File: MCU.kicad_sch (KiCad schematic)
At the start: 10 parts, among them SW1 SW_Omron_B3FS, SW3 SW_Omron_B3FS, U1 ESP32-WROOM-32E, X1 SG-3030CM

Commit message: Started to layout PCB
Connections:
- net MCU_EN is gone; now on net EN: C1.1, R1.2

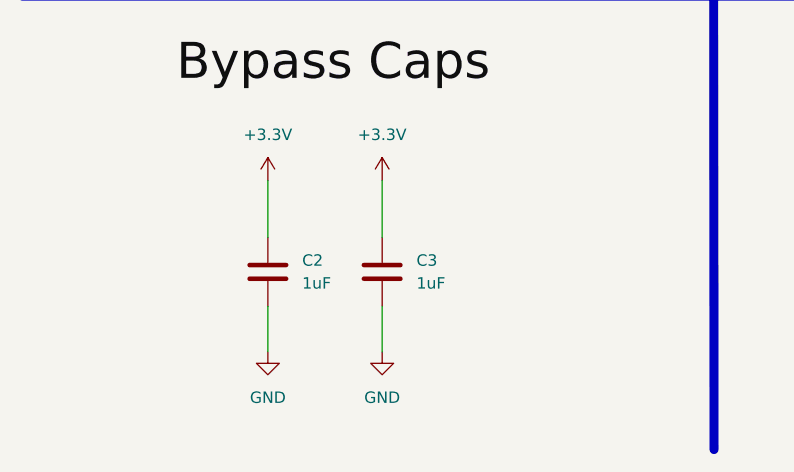
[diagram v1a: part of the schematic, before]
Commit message: Placed all components on PCB
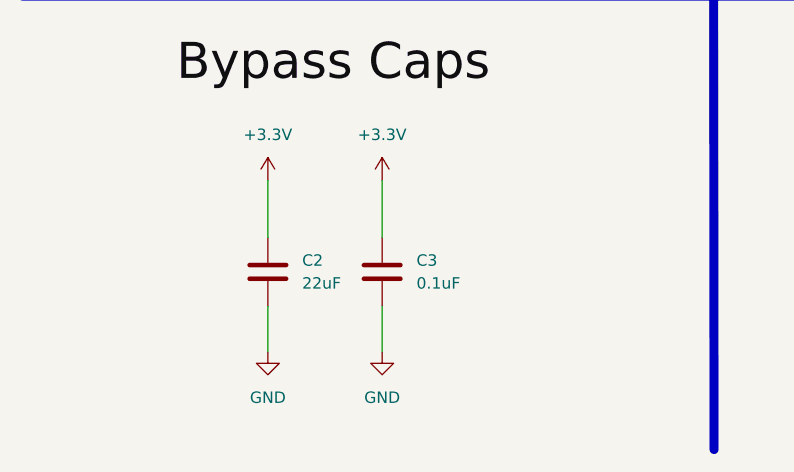
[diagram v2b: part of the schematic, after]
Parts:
- C2: value 1uF -> 22uF
- C3: value 1uF -> 0.1uF
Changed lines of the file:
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@@
 			)
 		)
-		(property "Value" "1uF"
+		(property "Value" "0.1uF"
 			(at 55.88 179.0699 0)
 			(effects
@@
 			)
 		)
-		(property "Value" "1uF"
+		(property "Value" "22uF"
 			(at 43.18 179.0699 0)
 			(effects

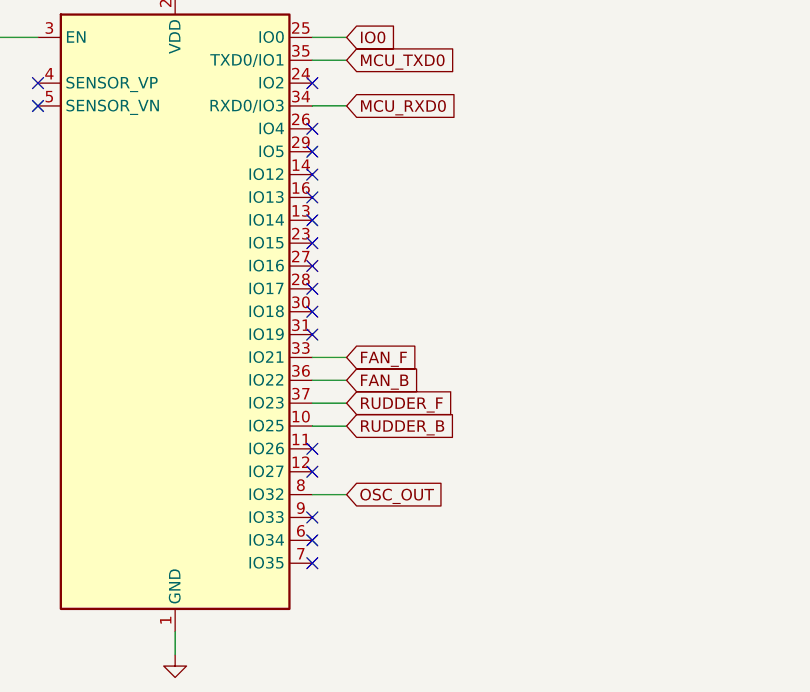
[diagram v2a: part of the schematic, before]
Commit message: Finished PCB routing
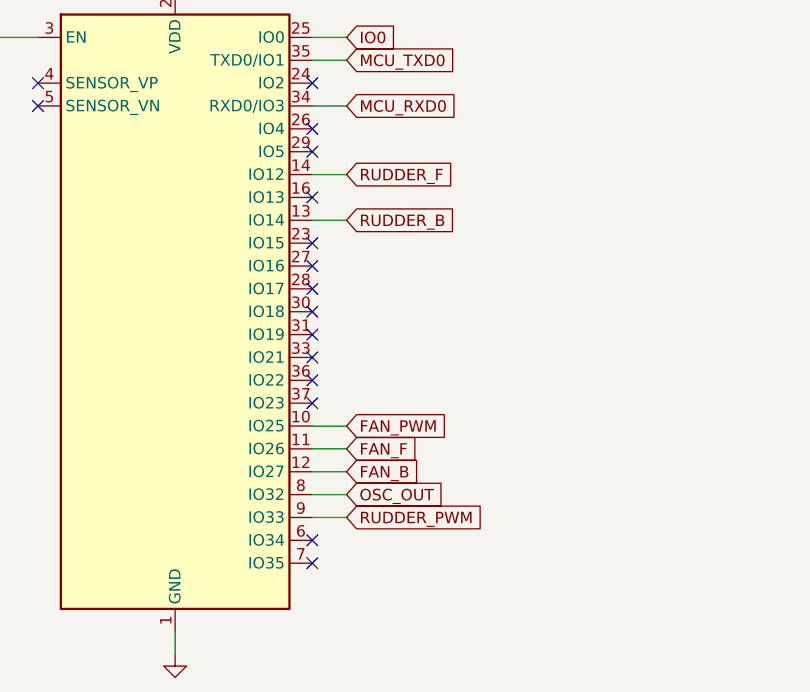
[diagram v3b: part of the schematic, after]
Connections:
- net FAN_B: now also U1.12 (IO27); no longer U1.36 (IO22)
- net FAN_F: now also U1.11 (IO26); no longer U1.33 (IO21)
- net RUDDER_B: now also U1.13 (IO14); no longer U1.10 (IO25)
- net RUDDER_F: now also U1.14 (IO12); no longer U1.37 (IO23)
- net RUDDER_PWM: now reaches U1.9 (IO33)
- new net FAN_PWM: U1.10 (IO25)
- no-connect marks 18 -> 16
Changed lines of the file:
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@@
+	)
+	(no_connect
+		(at 113.03 83.82)
 	)
 	(no_connect
@@
 	)
 	(no_connect
+		(at 113.03 99.06)
+	)
+	(no_connect
 		(at 82.55 66.04)
 	)
 	(no_connect
-		(at 113.03 83.82)
-	)
-	(no_connect
-		(at 113.03 106.68)
+		(at 113.03 81.28)
 	)
 	(no_connect
@@
 	)
 	(no_connect
-		(at 113.03 104.14)
+		(at 113.03 86.36)
 	)
 	(no_connect
-		(at 113.03 81.28)
+		(at 113.03 93.98)
 	)
 	(no_connect
-		(at 113.03 111.76)
+		(at 113.03 114.3)
+	)
+	(no_connect
+		(at 113.03 96.52)
+	)
+	(no_connect
+		(at 113.03 71.12)
 	)
 	(no_connect
@@
 	)
 	(no_connect
-		(at 113.03 78.74)
-	)
-	(no_connect
-		(at 113.03 114.3)
-	)
-	(no_connect
-		(at 113.03 71.12)
-	)
-	(no_connect
 		(at 113.03 68.58)
-	)
-	(no_connect
-		(at 113.03 73.66)
 	)
 	(no_connect
 		(at 113.03 116.84)
 	)
-	(no_connect
-		(at 113.03 86.36)
-	)
 	(wire
 		(pts
@@
 		)
 	)
+	(wire
+		(pts
+			(xy 113.03 78.74) (xy 116.84 78.74)
+		)
+		(stroke
+			(width 0)
+			(type default)
+		)
+	)
 	(polyline
 		(pts
@@
 	(wire
 		(pts
-			(xy 113.03 99.06) (xy 116.84 99.06)
-		)
-		(stroke
-			(width 0)
-			(type default)
-		)
-	)
-	(wire
-		(pts
 			(xy 39.37 181.61) (xy 39.37 186.69)
 		)
@@
 	(wire
 		(pts
+			(xy 113.03 106.68) (xy 116.84 106.68)
+		)
+		(stroke
+			(width 0)
+			(type default)
+		)
+	)
+	(wire
+		(pts
 			(xy 128.27 165.1) (xy 128.27 168.91)
 		)
@@
 	(wire
 		(pts
+			(xy 113.03 111.76) (xy 116.84 111.76)
+		)
+		(stroke
+			(width 0)
+			(type default)
+		)
+	)
+	(wire
+		(pts
+			(xy 113.03 104.14) (xy 116.84 104.14)
+		)
+		(stroke
+			(width 0)
+			(type default)
+		)
+	)
+	(wire
+		(pts
 			(xy 46.99 63.5) (xy 46.99 66.04)
 		)
@@
 	(wire
 		(pts
-			(xy 113.03 96.52) (xy 116.84 96.52)
-		)
-		(stroke
-			(width 0)
-			(type default)
-		)
-	)
-	(wire
-		(pts
-			(xy 113.03 93.98) (xy 116.84 93.98)
-		)
-		(stroke
-			(width 0)
-			(type default)
-		)
-	)
-	(wire
-		(pts
 			(xy 240.03 101.6) (xy 245.11 101.6)
 		)
@@
 		(pts
 			(xy 113.03 101.6) (xy 116.84 101.6)
+		)
+		(stroke
+			(width 0)
+			(type default)
+		)
+	)
+	(wire
+		(pts
+			(xy 113.03 73.66) (xy 116.84 73.66)
 		)
 		(stroke
@@
 		)
 	)
-	(global_label "RUDDER_F"
+	(global_label "RUDDER_PWM"
 		(shape input)
-		(at 116.84 99.06 0)
+		(at 116.84 111.76 0)
 		(fields_autoplaced yes)
 		(effects
@@
 		)
 		(property "Intersheetrefs" "${INTERSHEET_REFS}"
-			(at 129.4409 99.06 0)
+			(at 132.5251 111.76 0)
 			(effects
 				(font
@@
 	(global_label "RUDDER_B"
 		(shape input)
-		(at 116.84 101.6 0)
+		(at 116.84 78.74 0)
 		(fields_autoplaced yes)
 		(effects
@@
 		)
 		(property "Intersheetrefs" "${INTERSHEET_REFS}"
-			(at 129.6223 101.6 0)
+			(at 129.6223 78.74 0)
 			(effects
 				(font
@@
 		)
 	)
-	(global_label "FAN_F"
+	(global_label "FAN_B"
 		(shape input)
-		(at 116.84 93.98 0)
+		(at 116.84 106.68 0)
 		(fields_autoplaced yes)
 		(effects
@@
 		)
 		(property "Intersheetrefs" "${INTERSHEET_REFS}"
-			(at 125.3891 93.98 0)
+			(at 125.5705 106.68 0)
 			(effects
 				(font
@@
 		)
 	)
+	(global_label "FAN_F"
+		(shape input)
+		(at 116.84 104.14 0)
+		(fields_autoplaced yes)
+		(effects
+			(font
+				(size 1.27 1.27)
+			)
+			(justify left)
+		)
+		(property "Intersheetrefs" "${INTERSHEET_REFS}"
+			(at 125.3891 104.14 0)
+			(effects
+				(font
+					(size 1.27 1.27)
+				)
+				(justify left)
+				(hide yes)
+			)
+		)
+	)
 	(global_label "MCU_TXD0"
 		(shape input)
@@
 		)
 	)
-	(global_label "FAN_B"
+	(global_label "RUDDER_F"
 		(shape input)
-		(at 116.84 96.52 0)
+		(at 116.84 73.66 0)
 		(fields_autoplaced yes)
 		(effects
@@
 		)
 		(property "Intersheetrefs" "${INTERSHEET_REFS}"
-			(at 125.5705 96.52 0)
+			(at 129.4409 73.66 0)
 			(effects
 				(font
+					(size 1.27 1.27)
+				)
+				(justify left)
+				(hide yes)
+			)
+		)
+	)
+	(global_label "FAN_PWM"
+		(shape input)
+		(at 116.84 101.6 0)
+		(fields_autoplaced yes)
+		(effects
+			(font
+				(size 1.27 1.27)
+			)
+			(justify left)
+		)
+		(property "Intersheetrefs" "${INTERSHEET_REFS}"
+			(at 128.4733 101.6 0)
+			(effects
+				(font

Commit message: Updated PCB to be smaller and support stepper
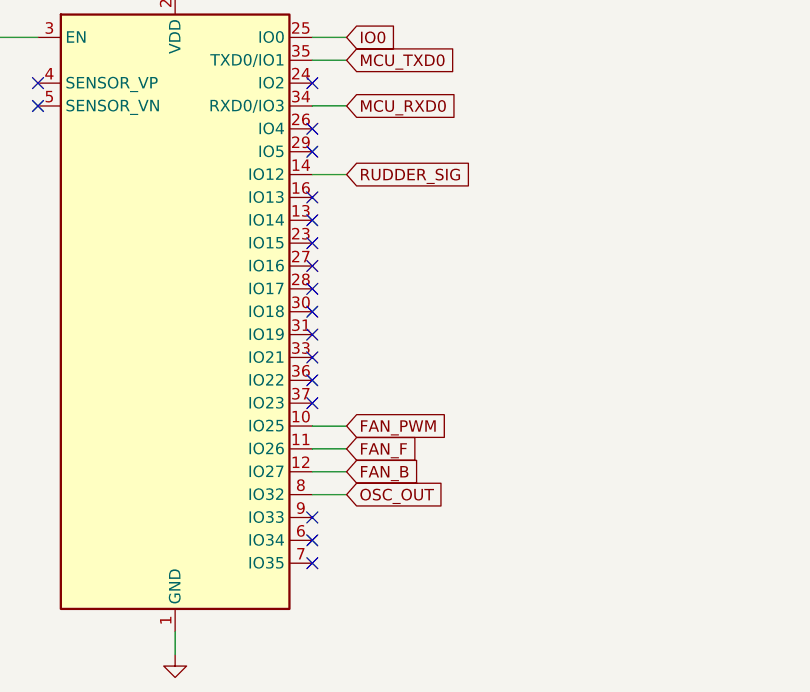
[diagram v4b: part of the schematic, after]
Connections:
- net RUDDER_B: no longer names the net of U1.13 (IO14)
- net RUDDER_F renamed RUDDER_SIG
- net RUDDER_PWM: no longer names the net of U1.9 (IO33)
- no-connect marks 16 -> 18
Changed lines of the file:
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@@
+	)
+	(no_connect
+		(at 113.03 78.74)
 	)
 	(no_connect
@@
 	)
 	(no_connect
+		(at 113.03 111.76)
+	)
+	(no_connect
 		(at 113.03 63.5)
 	)
@@
 		)
 	)
-	(wire
-		(pts
-			(xy 113.03 78.74) (xy 116.84 78.74)
-		)
-		(stroke
-			(width 0)
-			(type default)
-		)
-	)
 	(polyline
 		(pts
@@
 		(pts
 			(xy 232.41 69.85) (xy 240.03 69.85)
-		)
-		(stroke
-			(width 0)
-			(type default)
-		)
-	)
-	(wire
-		(pts
-			(xy 113.03 111.76) (xy 116.84 111.76)
 		)
 		(stroke
@@
 		)
 	)
-	(global_label "RUDDER_PWM"
-		(shape input)
-		(at 116.84 111.76 0)
-		(fields_autoplaced yes)
-		(effects
-			(font
-				(size 1.27 1.27)
-			)
-			(justify left)
-		)
-		(property "Intersheetrefs" "${INTERSHEET_REFS}"
-			(at 132.5251 111.76 0)
-			(effects
-				(font
-					(size 1.27 1.27)
-				)
-				(justify left)
-				(hide yes)
-			)
-		)
-	)
-	(global_label "RUDDER_B"
-		(shape input)
-		(at 116.84 78.74 0)
-		(fields_autoplaced yes)
-		(effects
-			(font
-				(size 1.27 1.27)
-			)
-			(justify left)
-		)
-		(property "Intersheetrefs" "${INTERSHEET_REFS}"
-			(at 129.6223 78.74 0)
-			(effects
-				(font
-					(size 1.27 1.27)
-				)
-				(justify left)
-				(hide yes)
-			)
-		)
-	)
 	(global_label "FAN_B"
 		(shape input)
@@
 		)
 	)
-	(global_label "RUDDER_F"
+	(global_label "RUDDER_SIG"
 		(shape input)
 		(at 116.84 73.66 0)
@@
 		)
 		(property "Intersheetrefs" "${INTERSHEET_REFS}"
-			(at 129.4409 73.66 0)
+			(at 131.4366 73.66 0)
 			(effects
 				(font
